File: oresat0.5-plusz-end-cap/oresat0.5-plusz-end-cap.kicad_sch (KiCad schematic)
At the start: 35 parts, among them J2 U.FL-R-SMA, U1 LTC4305, U2 MMC5883MA, U3 MMC5883MA

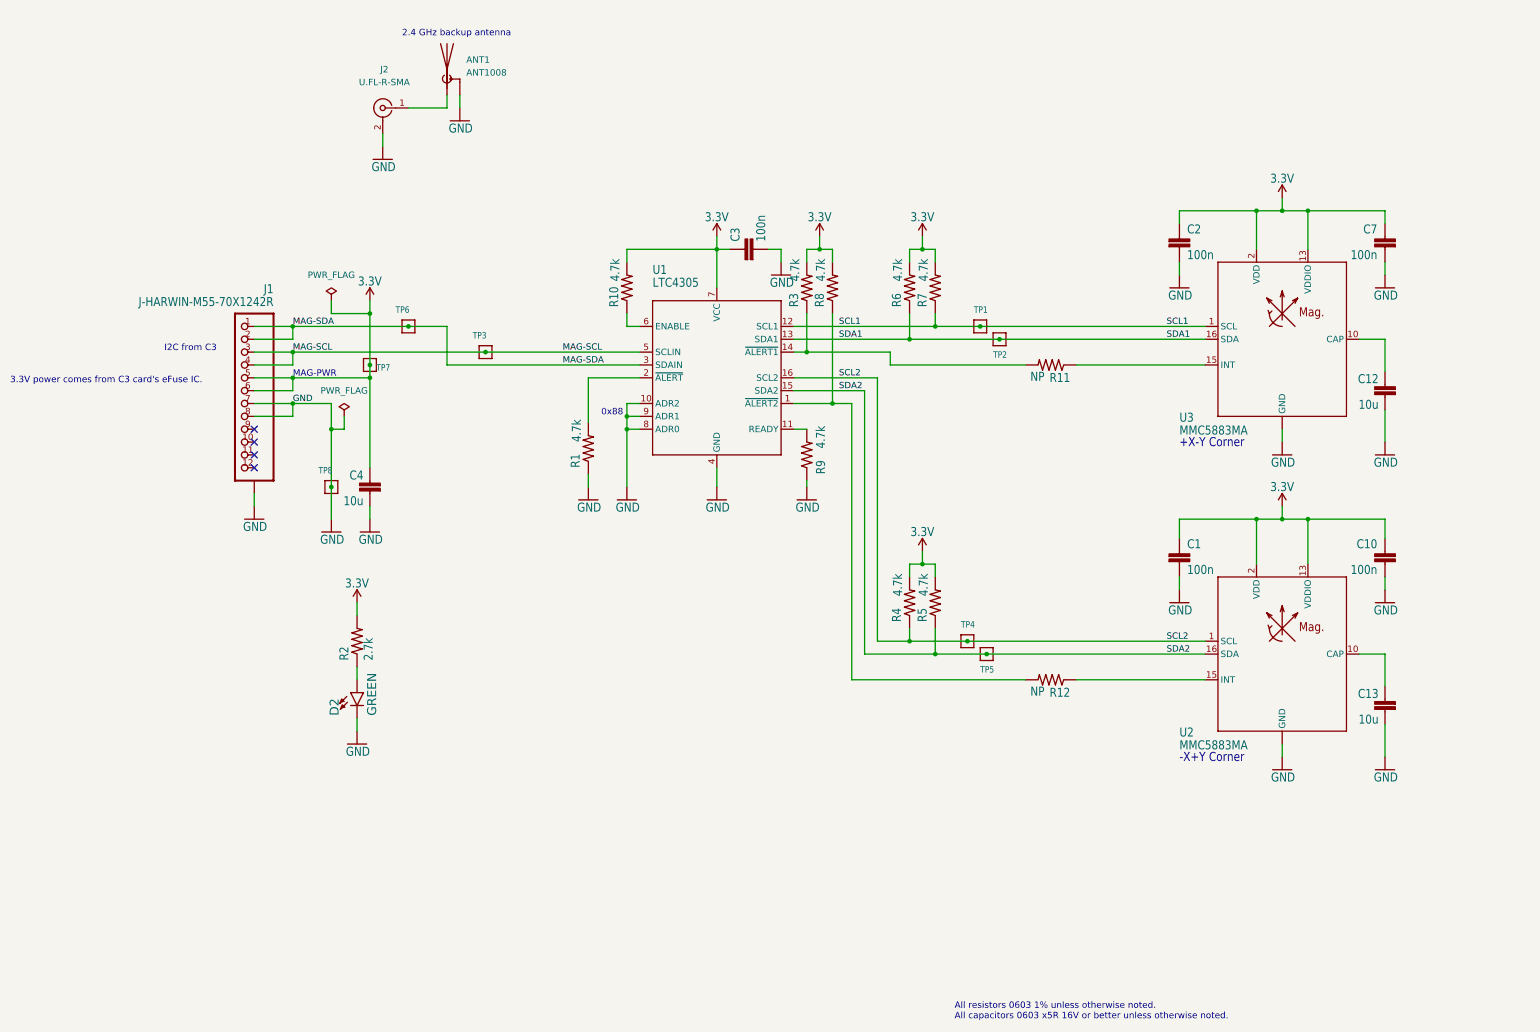
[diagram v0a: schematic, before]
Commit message: updated mmc5883 magnetometer to mmc5983 for both OreSat 0.5 +Z and -Z endcaps
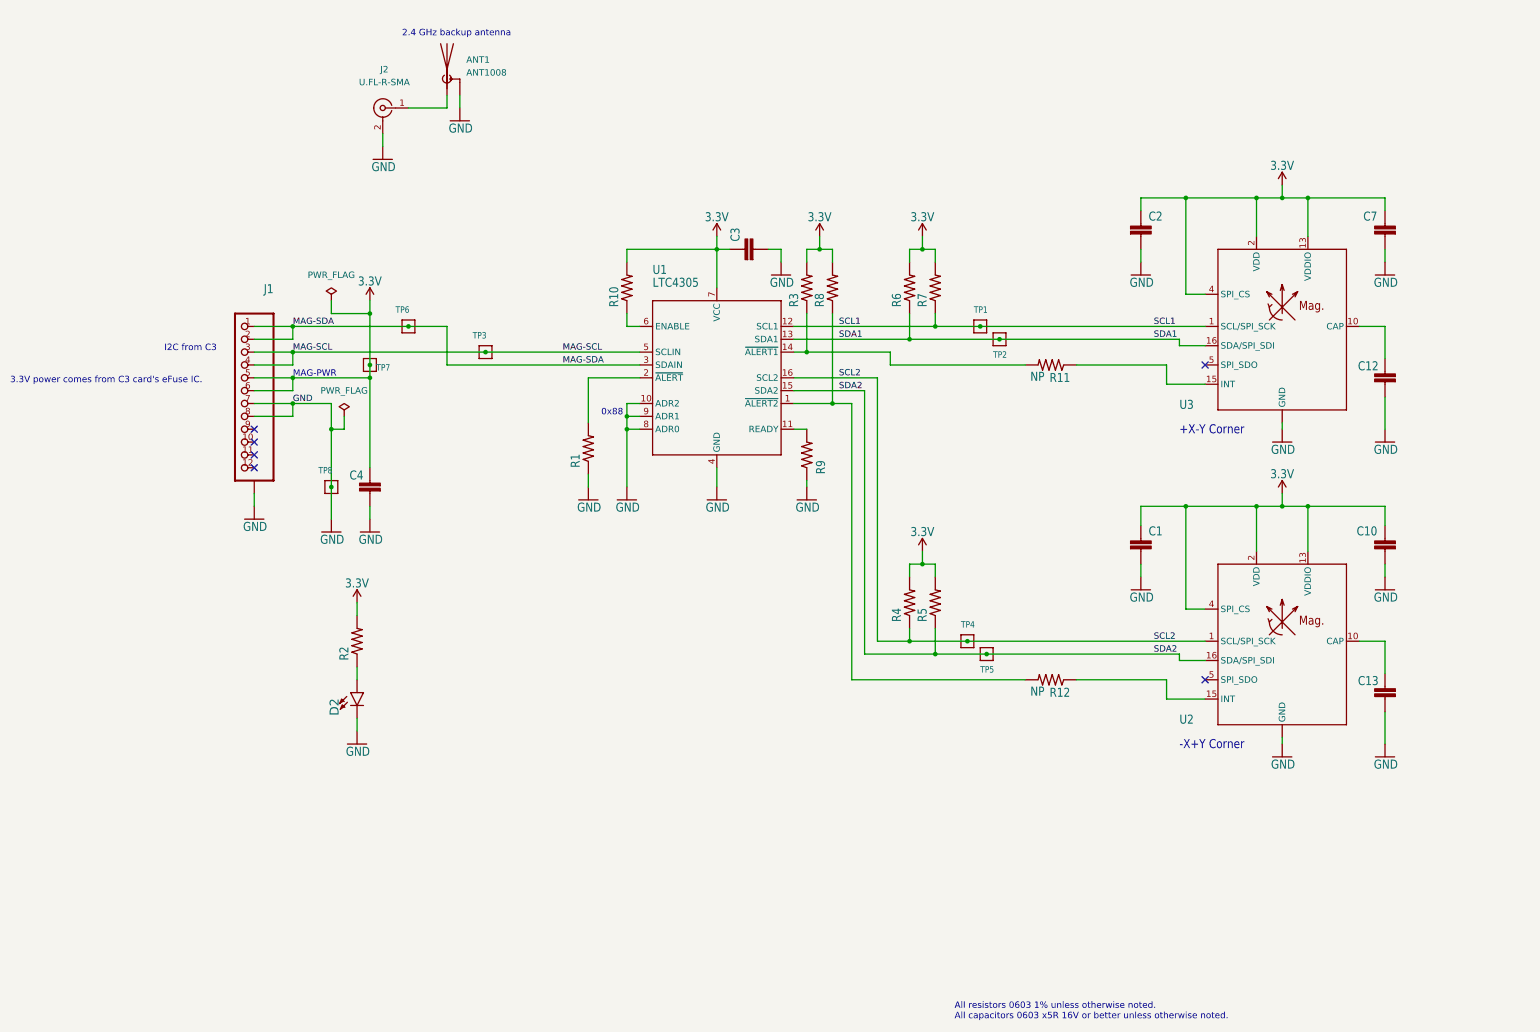
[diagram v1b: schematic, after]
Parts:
- C1, C10, C12, C13, C2, C3, C4, C7, D2, J1, R1, R10, R2, R3, R4, R5, R6, R7, R8, R9: value (none) -> ~
- U2, U3: value MMC5883MA -> MMC5983MA; footprint oresat0.5-plusz-end-cap:LGA-16(3X3) -> oresat-ics:LGA-16(3X3); symbol oresat0.5-plusz-end-cap-eagle-import:MMC5883MA -> oresat-ics:MMC5983MA
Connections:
- net 3.3V: now also U2.4 (SPI_CS), U3.4 (SPI_CS)
- no-connect marks 4 -> 6
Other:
- moved on the sheet: C1, C10, C12, C13, C2, C7

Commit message: Oresat 0.5 +z end cap v1.3 ready for ordering!
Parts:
- C1, C10, C2, C3, C7: value ~ -> 100n
- C12, C13, C4: value ~ -> 10u
- D2, J1, R1, R10, R3, R4, R5, R6, R7, R8, R9: value ~ -> 4.7k
- R2: value ~ -> 2.7k
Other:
- moved on the sheet: R10, R3, R8

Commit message: OreSat 0.5 Endcaps (+Z v1.3 and -Z v1.2) ready for ordering, reviewed -Z endcap, made small library and neatness changes to +Z endcap
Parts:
- R11, R12: value NP -> 2.7k; now not fitted
- U1: footprint oresat0.5-plusz-end-cap:16-SSOP -> oresat-ics:16-SSOP; symbol oresat0.5-plusz-end-cap-eagle-import:LTC4305 -> oresat-ics:LTC4305
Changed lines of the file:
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@@
 		(in_bom yes)
 		(on_board yes)
-		(dnp no)
+		(dnp yes)
 		(property "Reference" "R11"
 			(at 260.35 133.5786 0)
@@
 			)
 		)
-		(property "Value" "NP"
+		(property "Value" "2.7k"
 			(at 255.27 133.35 0)
 			(effects
@@
 		(in_bom yes)
 		(on_board yes)
-		(dnp no)
+		(dnp yes)
 		(property "Reference" "R12"
 			(at 260.35 195.8086 0)
@@
 			)
 		)
-		(property "Value" "NP"
+		(property "Value" "2.7k"
 			(at 255.27 195.58 0)
 			(effects
@@
 	)
 	(symbol
-		(lib_id "oresat0.5-plusz-end-cap-eagle-import:LTC4305")
+		(lib_id "oresat-ics:LTC4305")
 		(at 190.5 134.62 0)
 		(unit 1)
@@
 			)
 		)
-		(property "Footprint" "oresat0.5-plusz-end-cap:16-SSOP"
+		(property "Footprint" "oresat-ics:16-SSOP"
 			(at 190.5 134.62 0)
 			(effects

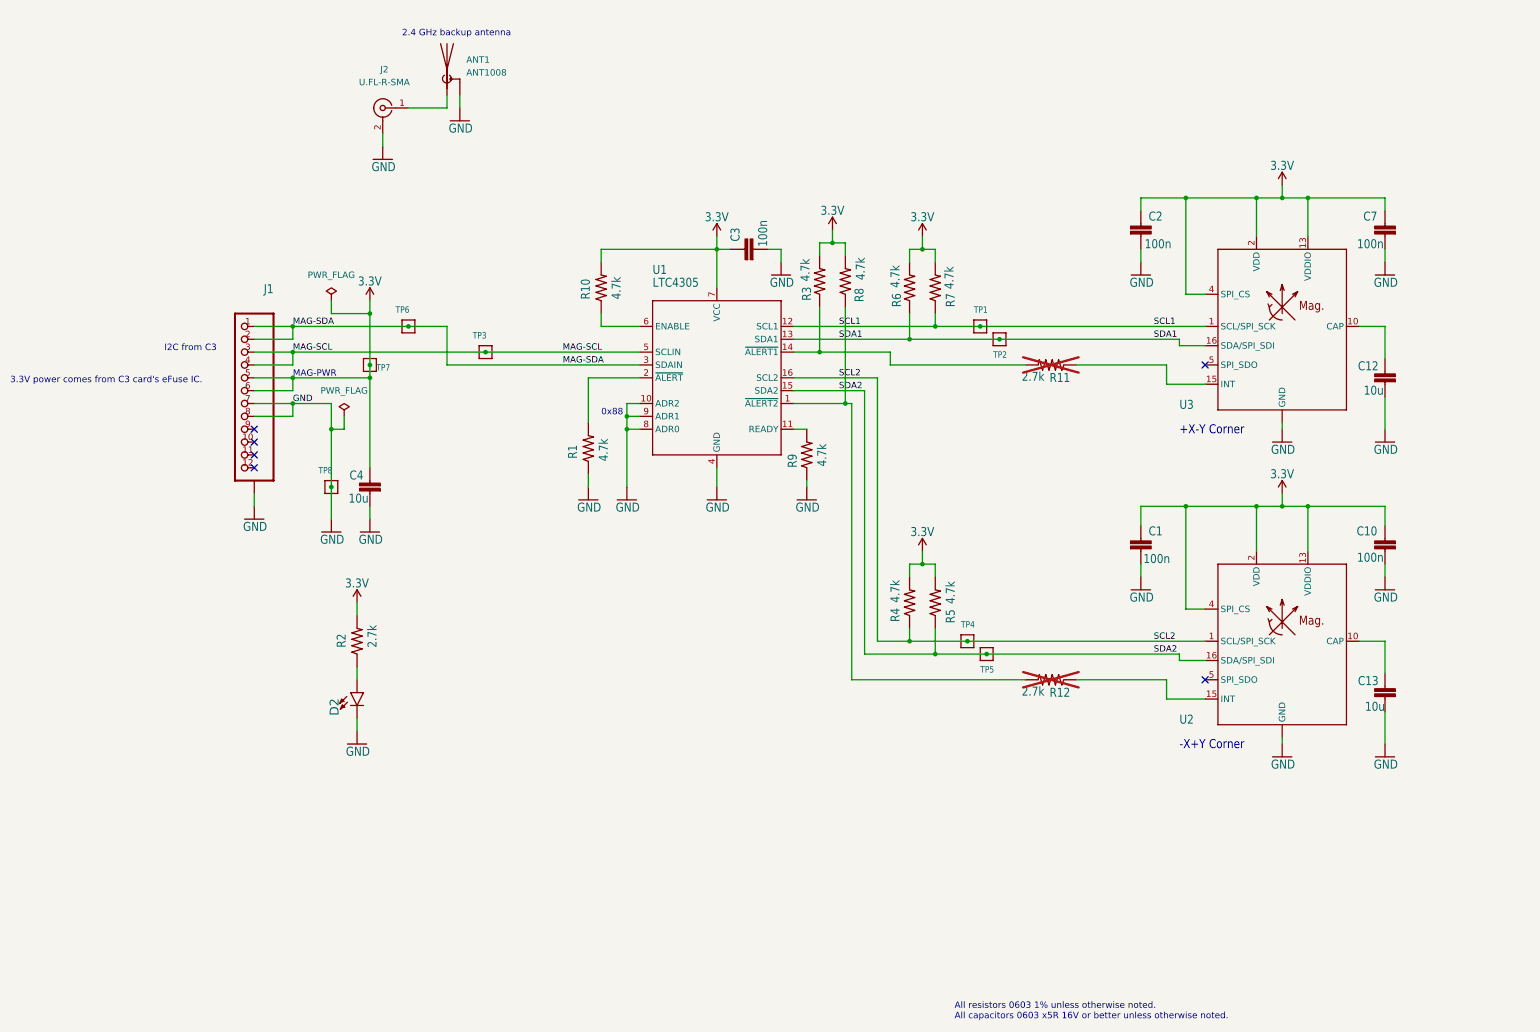
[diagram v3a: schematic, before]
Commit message: Fixed issues 5 and 6 -- weird 4.7k values everywhere, missing libraries, and used no-place to indicate actual no place components.
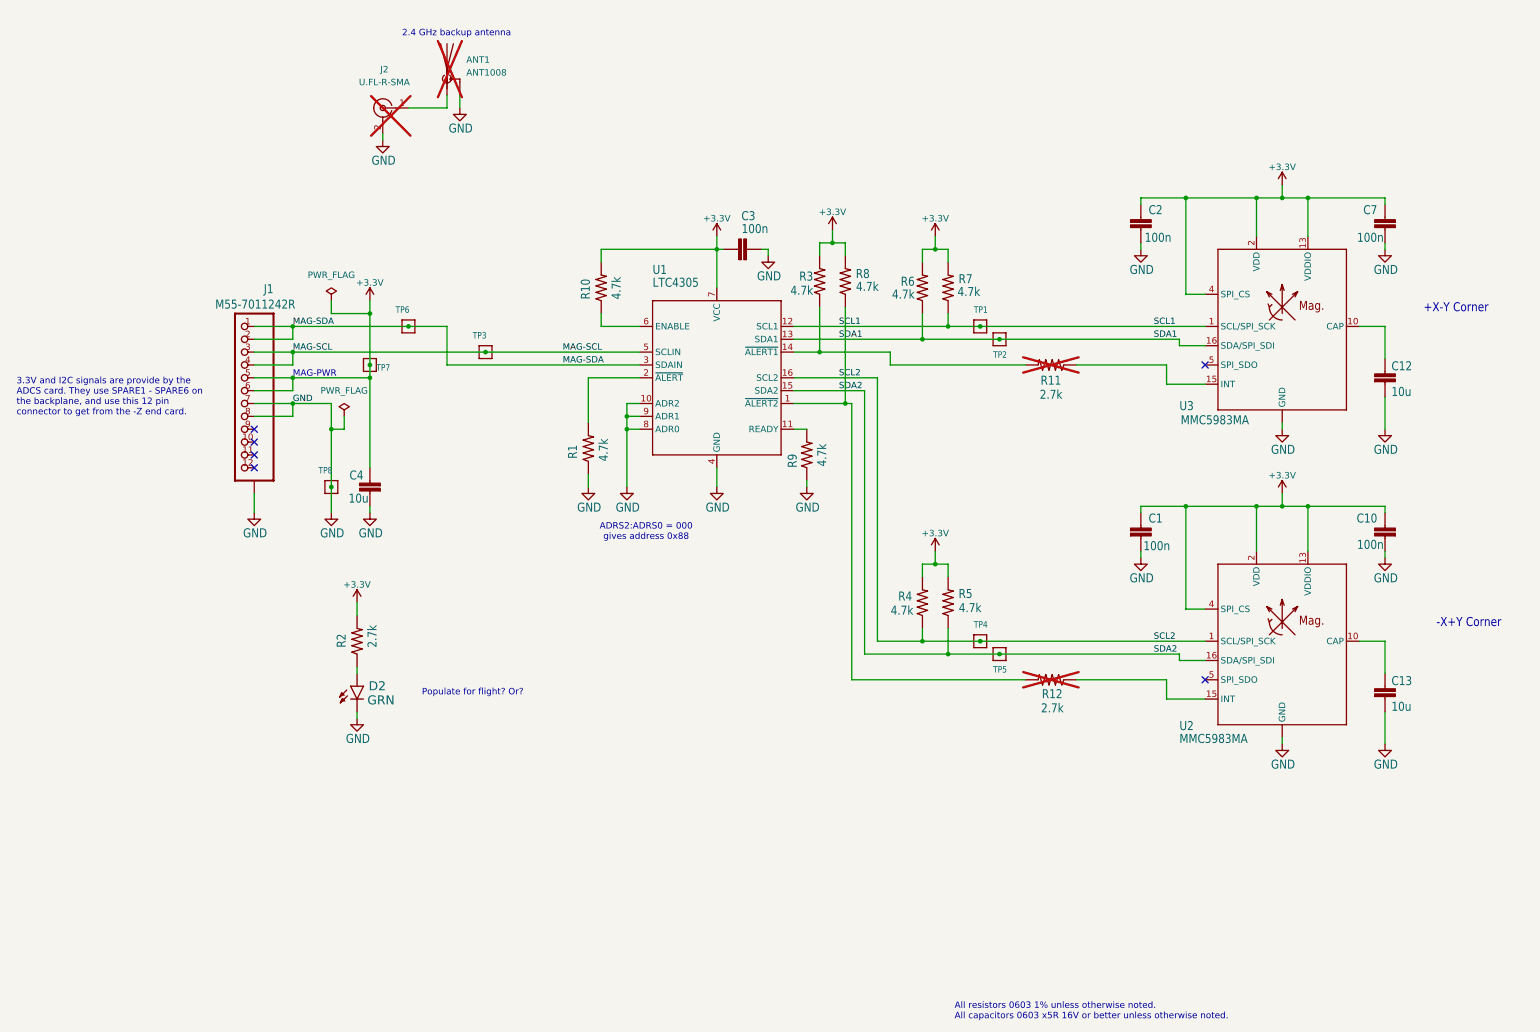
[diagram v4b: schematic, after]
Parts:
- ANT1, J2: now not fitted
- D2: value 4.7k -> GRN
- J1: value 4.7k -> M55-7011242R
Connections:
- net 3.3V renamed +3.3V
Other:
- note added: "3.3V and I2C signals are provide by the ADCS card. They use SPARE1 - SPARE6 on the backplane, and use this 12 pin connector to get from the -Z end card."
- note added: "ADRS2:ADRS0 = 000 gives address 0x88"
- note added: "Populate for flight? Or?"
- note removed: "0x88"
- note removed: "3.3V power comes from C3 card's eFuse IC."
- note removed: "I2C from C3"
- moved on the sheet: C1, C10, C2, C3, C7, D2, R4, R5, R6, R7, TP4, TP5

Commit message: Added note on which MAG was which for firmware (PZ1 - MZ2).
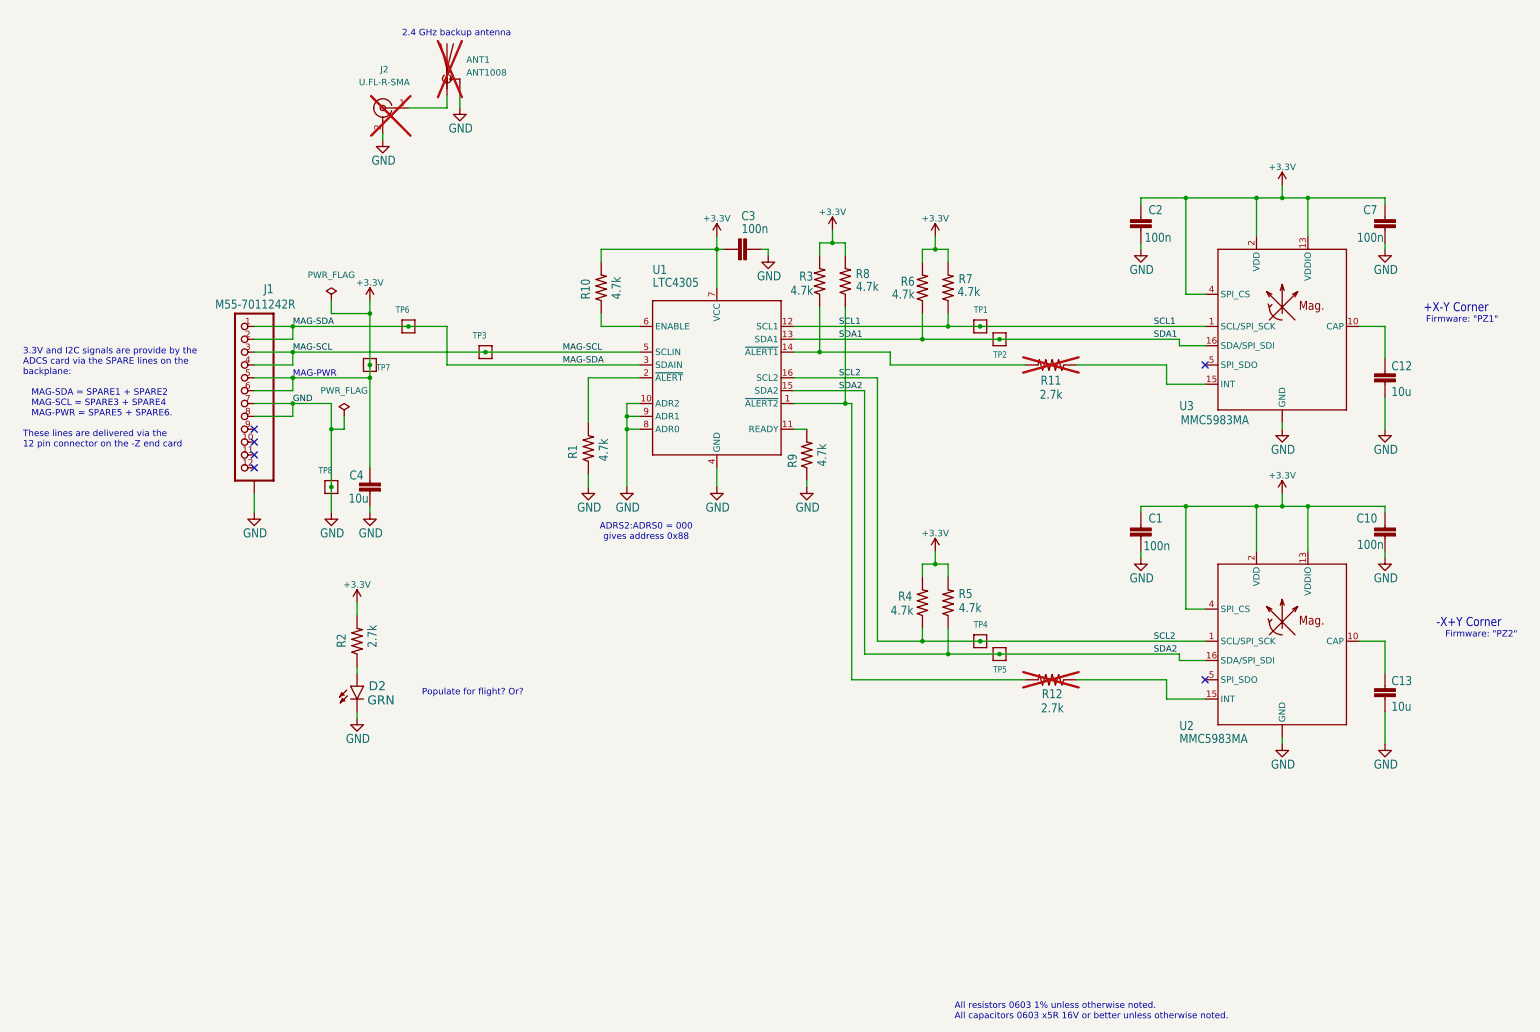
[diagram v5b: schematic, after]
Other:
- note added: "3.3V and I2C signals are provide by the ADCS card via the SPARE lines on the backplane: MAG-SDA = SPARE1 + SPARE2 MAG-SCL = SPARE3 + SPARE4 MAG-PWR = SPARE5 + SPARE6. These lines are delivered via the 12 pin connector on the -Z end card"
- note added: "Firmware: "PZ1""
- note added: "Firmware: "PZ2""
- note removed: "3.3V and I2C signals are provide by the ADCS card. They use SPARE1 - SPARE6 on the backplane, and use this 12 pin connector to get from the -Z end card."
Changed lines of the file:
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@@
+		)
+	)
+	(text "Firmware: \"PZ2\""
+		(exclude_from_sim no)
+		(at 341.63 185.42 0)
+		(effects
+			(font
+				(size 1.27 1.27)
+			)
 		)
 	)
@@
 		)
 	)
-	(text "3.3V and I2C signals are provide by the\nADCS card. They use SPARE1 - SPARE6 on \nthe backplane, and use this 12 pin \nconnector to get from the -Z end card."
+	(text "Firmware: \"PZ1\""
 		(exclude_from_sim no)
-		(at 52.07 142.24 0)
+		(at 337.82 123.19 0)
 		(effects
 			(font
+				(size 1.27 1.27)
+			)
+		)
+	)
+	(text "3.3V and I2C signals are provide by the \nADCS card via the SPARE lines on the \nbackplane:\n\n   MAG-SDA = SPARE1 + SPARE2\n   MAG-SCL = SPARE3 + SPARE4 \n   MAG-PWR = SPARE5 + SPARE6.\n\nThese lines are delivered via the \n12 pin connector on the -Z end card"
+		(exclude_from_sim no)
+		(at 53.34 148.59 0)
+		(effects
+			(font

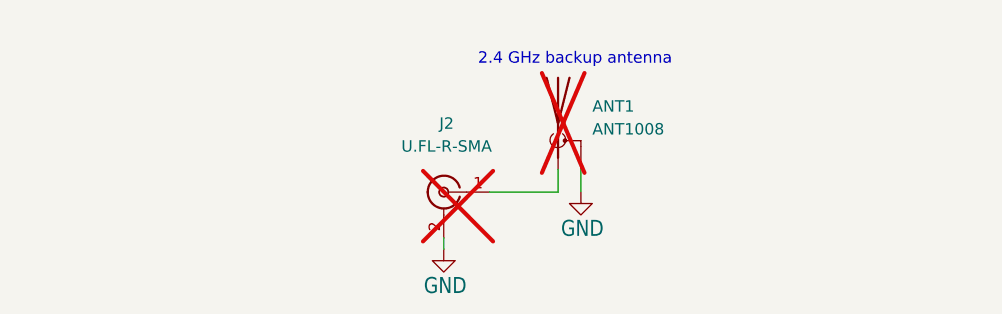
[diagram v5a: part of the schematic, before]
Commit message: More information on end cap RF, including coax jumper for end cap.
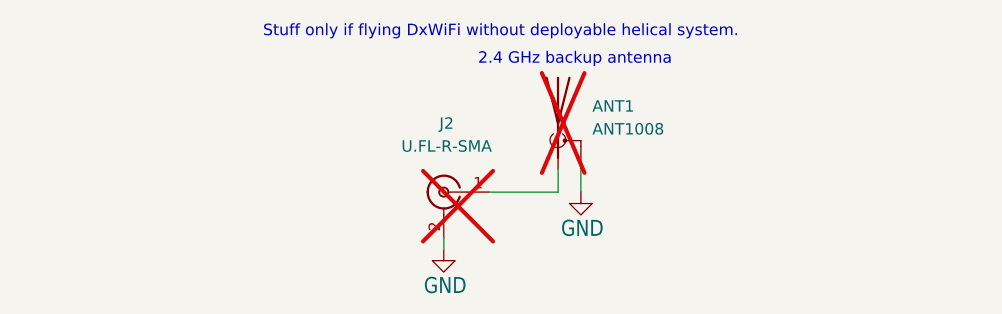
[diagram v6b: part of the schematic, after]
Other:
- note added: "Stuff only if flying DxWiFi without deployable helical system."
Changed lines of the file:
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@@
+		)
+	)
+	(text "Stuff only if flying DxWiFi without deployable helical system."
+		(exclude_from_sim no)
+		(at 130.81 63.5 0)
+		(effects
+			(font
+				(size 1.27 1.27)
+			)
 		)
 	)
